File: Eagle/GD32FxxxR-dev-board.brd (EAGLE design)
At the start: 52.4 x 55.9 mm, 50 parts, among them J1 USART0, J2 VBat, J3 USB, J4 I2C1, J5 GPIOC, Q1 25MHz, Q2 32.768KHz, SW1 RESET, SW2 BOOT0, U1 GD32F207RX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

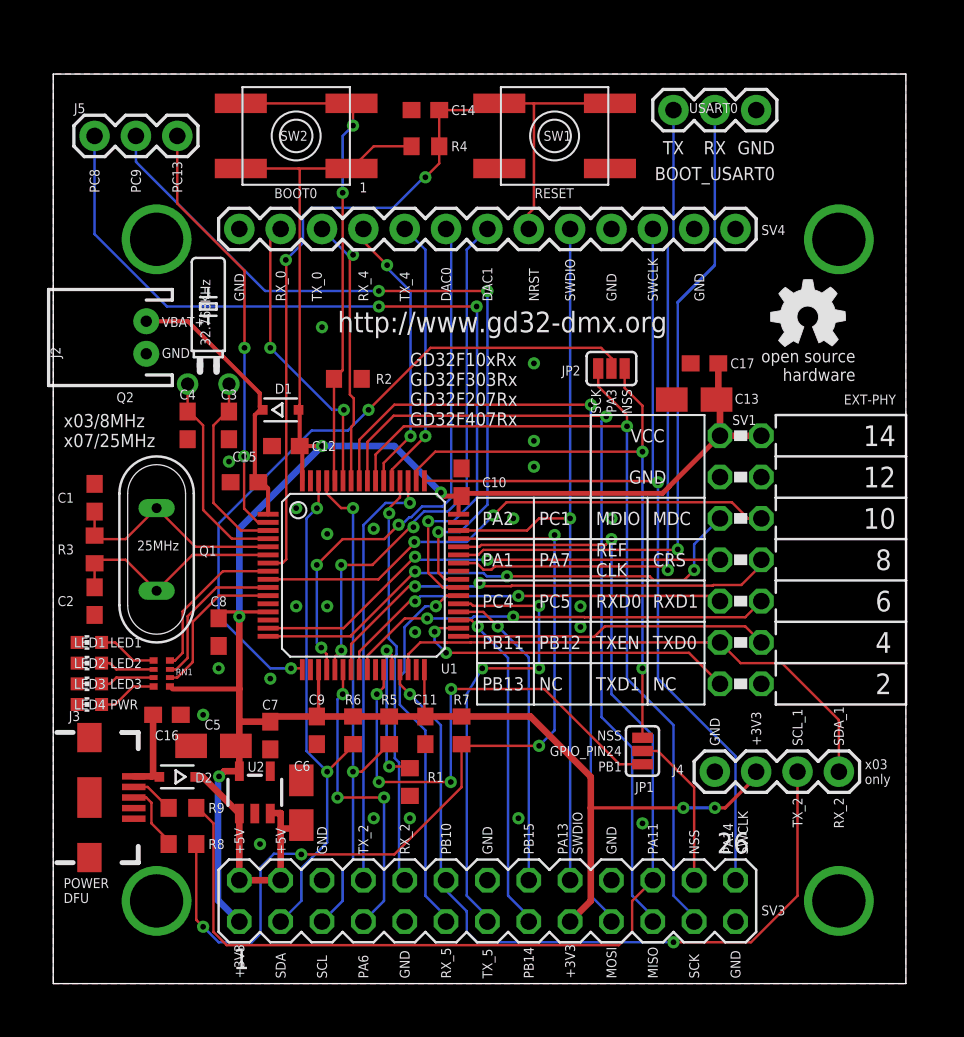
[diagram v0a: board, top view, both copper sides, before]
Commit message: Updated Add-on Pixel 8x 4 Universes
*. Added support for clock based led chip's (for example APA102)
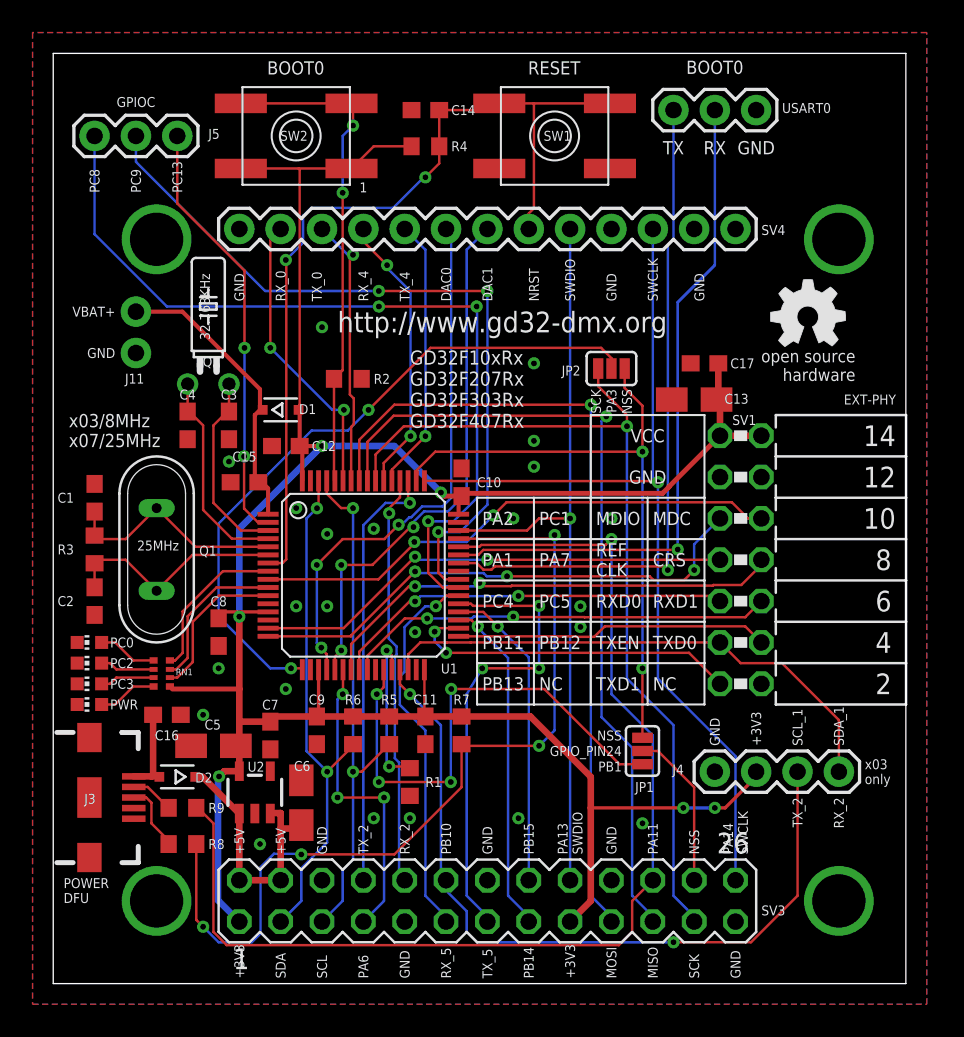
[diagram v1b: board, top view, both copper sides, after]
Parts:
- removed J2: VBat, SparkFun-Connectors:JST-2-PTH
- added J11: Vbat, SparkFun-Connectors:1X02_NO_SILK
- LED1: value LED1 -> PC0
- LED2: value LED2 -> PC2
- LED3: value LED3 -> PC3
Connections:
- net GND: now also J11.1; no longer J2.1
- net VBAT: now also J11.2; no longer J2.2
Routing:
- net VBAT: track 17.2 -> 18.2 mm
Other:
- board size 52.4 x 55.9 mm -> 52.4 x 57.1 mm
- board text added: "BOOT0"
- board text added: "GD32F10xRx GD32F207Rx GD32F303Rx GD32F407Rx"
- board text removed: "BOOT_USART0"
- board text removed: "GD32F10xRx GD32F303Rx GD32F207Rx GD32F407Rx"

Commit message: Added SPI Flash ROM
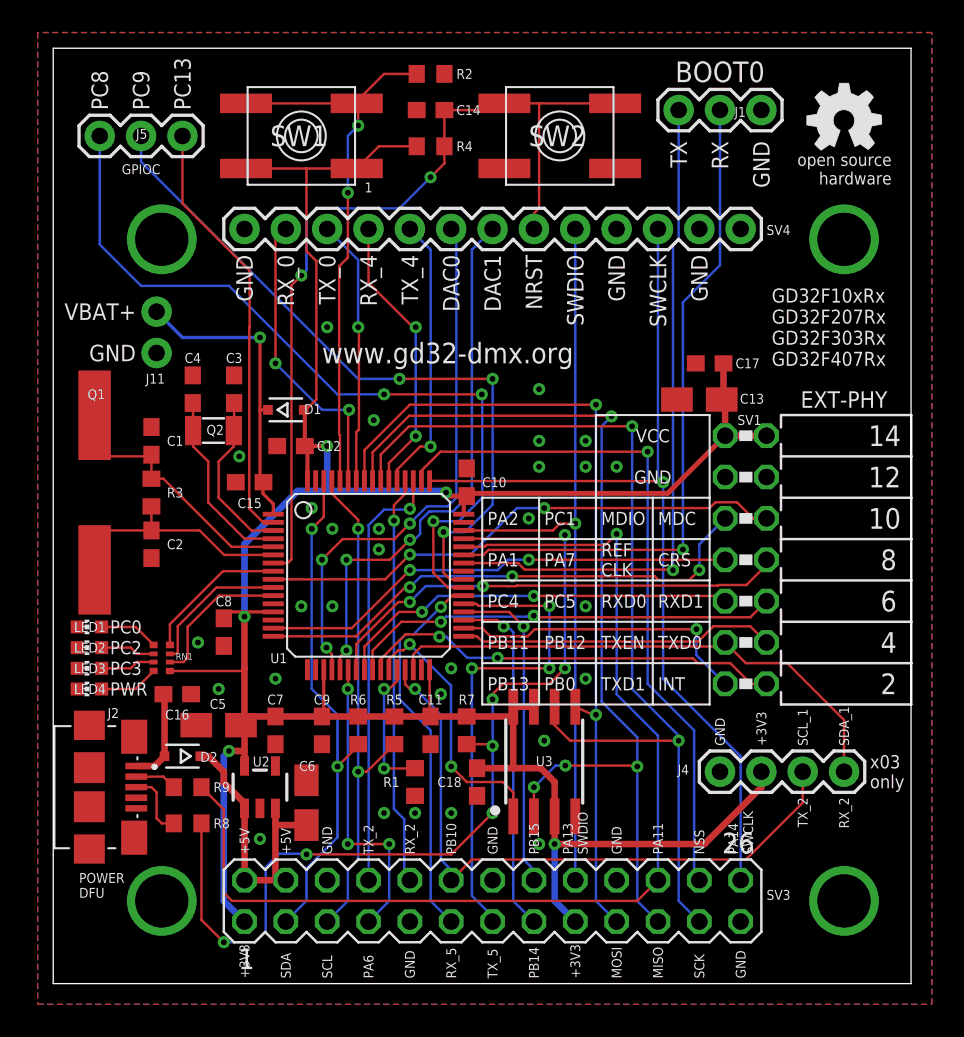
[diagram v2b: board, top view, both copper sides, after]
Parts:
- removed J3: USB, USB-micro:USB-B-MICRO-SMD
- removed JP1: GPIO_PIN24, SparkFun-Jumpers:SMT-JUMPER_3_1-NC_PASTE_SILK
- removed JP2: PA3, SparkFun-Jumpers:SMT-JUMPER_3_1-NC_PASTE_SILK
- added C18: 100n, rcl:C0603
- added J2: 10118192-0002LF, USB connector:10118192-0002LF
- added U3: W25Q128JVSIQ, SparkFun-IC-Memory:SO08-EIAJ
- C3, C4: value 10pF -> 12pF
- J1: value USART0 -> BOOT0
- Q1: value 25MHz -> 8/25 MHz; device special:QS -> crystal:CSM-7X-DU
- Q2: value 32.768KHz -> 32.768kHz; device crystal:TC26H -> crystal-geyer_V1_0:3.2X1.5
- SW1: value RESET -> BOOT0
- SW2: value BOOT0 -> RESET
- moved R2 19.4 mm to (23.2, 55.9)
- moved SW2 16.2 mm to (31.1, 52.1)
- moved SW1 15.6 mm to (15.2, 52.1)
- moved GOLD_ORB_SM1 12.3 mm to (48.6, 53.0)
- moved Q1 5.17 mm to (2.54, 30.2)
- moved C1 4.94 mm to (6.03, 33.3)
- moved C2 4.94 mm to (6.03, 27.0)
- moved R3 4.94 mm to (6.03, 30.2), turned to 270 degrees
- moved Q2 2.88 mm to (9.84, 34.0)
- moved C3 2.25 mm to (11.1, 36.5), turned to 270 degrees
- moved C4 2.25 mm to (8.57, 36.5), turned to 270 degrees
- moved C16 1.42 mm to (7.62, 17.8)
- moved D2 1.31 mm to (7.94, 14.0)
- moved C5 1.31 mm to (10.2, 15.9)
- moved R8 1.31 mm to (8.26, 9.84)
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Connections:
- net DAC0 renamed PA4/DAC0
- net DAC1 renamed PA5/DAC1
- removed net GPIO_PIN24: JP1.2, SV3.24
- removed net PA3: JP2.2, U1.17
- removed net PA8: U1.41
- net +3V3: now also C18.1, SW1.A, SW1.A', U3.3, U3.7, U3.8; no longer SW2.A, SW2.A'
- net BOOT0: now also SW1.B, SW1.B'; no longer SW2.B, SW2.B'
- net D+: now also J2.3; no longer J3.D+
- net D-: now also J2.2; no longer J3.D-
- net GND: now also C18.2, J2.4, J2.5, J2.SH1, J2.SH2, J2.SH3, J2.SH4, J2.SH5, J2.SH6, SW2.A, SW2.A', U3.4; no longer J3.GND, J3.ID, J3.SHIELD1, J3.SHIELD2, J3.SHIELD3, SW1.A, SW1.A'
- net NRST: now also SW2.B, SW2.B'; no longer SW1.B, SW1.B'
- net OSC_IN: now also R3.1; no longer R3.2
- net OSC_OUT: now also R3.2; no longer R3.1
- net PB1: now also U3.1; no longer JP1.1
- net PHY_INT: now also SV1.2
- net SPI2_MISO: now also U3.2
- net SPI2_MOSI: now also U3.5
- net SPI2_NSS: now also SV3.24; no longer JP1.3, JP2.3
- net SPI2_SCK: now also U3.6; no longer JP2.1
- net VBUS: now also J2.1; no longer J3.VBUS
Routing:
- net PA3: track 41.7 -> 0.00 mm, vias 2 -> 0
- net PHY_INT: track 0.00 -> 26.2 mm, vias 0 -> 2
- net PB1: track 31.0 -> 16.8 mm, vias 4 -> 2
- net GPIO_PIN24: track 9.81 -> 0.00 mm
- net +3V3: track 158.9 -> 167.5 mm, vias 6 -> 5
- net SPI2_MISO: track 50.2 -> 58.8 mm, vias 1 -> 4
- net PB10: track 47.2 -> 39.8 mm, vias 2 -> 1
- net SPI2_SCK: track 54.2 -> 59.1 mm, vias 1 -> 2
- net BOOT0: track 30.5 -> 35.1 mm
- net SPI2_NSS: track 38.1 -> 42.6 mm, vias 2 -> 1
- net PA12: track 54.6 -> 58.5 mm, vias 4 -> 7
- net PA11: track 69.8 -> 66.5 mm
- net BOOT_RX: track 44.8 -> 41.5 mm
- net PC9: track 47.2 -> 44.1 mm
- net PC8: track 52.1 -> 49.3 mm
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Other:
- board size 52.4 x 57.1 mm -> 52.7 x 57.5 mm
- board text added: "INT"
- board text added: "PB0"
- board text added: "www.gd32-dmx.org"
- board text removed: "BOOT0"
- board text removed: "GPIO_PIN24"
- board text removed: "NC"
- board text removed: "PA3"
- board text removed: "PB1"
- board text removed: "http://www.gd32-dmx.org"
- board text removed: "x03/8MHz x07/25MHz"
